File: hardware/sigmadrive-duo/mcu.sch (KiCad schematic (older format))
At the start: 107 parts, among them J1 CONN_02X02, J2 CONN_02X05, J3 Conn_02x03_Odd_Even, J4 CONN_02X02, J5 Conn_02x03_Odd_Even, J6 629_105_150_921, M1_SW1 CONN_02X02, M1_SW2 CONN_02X02, M2_SW1 CONN_02X02, M2_SW2 CONN_02X02, SW2 SW_DIP_x04, U12 SN65HVD75DGKR, U3 SN65HVD75DGKR, U4 TPD4S009, U5 STM32F745VGTx, U6 TPD4S009, U8 SN65HVD75DGKR, Y1 NX3225SA-12.000M-STD-CSR-1

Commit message: Sigmadrive-duo final HW update
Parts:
- R88: value 100 -> 120
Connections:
- net DRV_SDO: now also U5.17 (ADC1_IN12/ADC2_IN12/ADC3_IN12/ETH_TXD2/FMC_SDNE0/SPI2_MISO/USB_OTG_HS_ULPI_DIR/PC2); no longer U5.18 (ADC1_IN13/ADC2_IN13/ADC3_IN13/ETH_TX_CLK/FMC_SDCKE0/I2S2_SD/SPI2_MOSI/USB_OTG_HS_ULPI_NXT/PC3)
- net M1_IA_FB: now also U4.4 (D2+), U4.7 (D2+); no longer U4.1 (D1+), U4.10 (D1+)
- net M1_IC_FB: now also U4.1 (D1+), U4.10 (D1+); no longer U4.4 (D2+), U4.7 (D2+)
- net ADC1_IN4 renamed ADC3_IN3
- net ADC3_IN3: now also U5.25 (ADC1_IN3/ADC2_IN3/ADC3_IN3/ETH_COL/TIM2_CH4/TIM5_CH4/TIM9_CH2/USART2_RX/USB_OTG_HS_ULPI_D0/PA3); no longer U5.28 (ADC1_IN4/ADC2_IN4/DAC_OUT1/DCMI_HSYNC/I2S1_WS/I2S3_WS/SPI1_NSS/SPI3_NSS/USART2_CK/USB_OTG_HS_SOF/PA4)
- net PA3 renamed PA4
- net PA4: now also U5.28 (ADC1_IN4/ADC2_IN4/DAC_OUT1/DCMI_HSYNC/I2S1_WS/I2S3_WS/SPI1_NSS/SPI3_NSS/USART2_CK/USB_OTG_HS_SOF/PA4); no longer U5.25 (ADC1_IN3/ADC2_IN3/ADC3_IN3/ETH_COL/TIM2_CH4/TIM5_CH4/TIM9_CH2/USART2_RX/USB_OTG_HS_ULPI_D0/PA3)
- net PC2 renamed PC3
- net PC3: now also U5.18 (ADC1_IN13/ADC2_IN13/ADC3_IN13/ETH_TX_CLK/FMC_SDCKE0/I2S2_SD/SPI2_MOSI/USB_OTG_HS_ULPI_NXT/PC3); no longer U5.17 (ADC1_IN12/ADC2_IN12/ADC3_IN12/ETH_TXD2/FMC_SDNE0/SPI2_MISO/USB_OTG_HS_ULPI_DIR/PC2)
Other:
- note removed: "Swapped in Duo\nPE14 <--> PE15\n"
- moved on the sheet: R31, R43
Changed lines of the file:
@@
 Wire Wire Line
 	7200 13900 7200 14050
-Text HLabel 22300 3850 2    60   Input ~ 0
+Text HLabel 22300 3950 2    60   Input ~ 0
 M1_IC_FB
 Text HLabel 22300 3650 2    60   Input ~ 0
@@
 Text HLabel 22300 3750 2    60   Input ~ 0
 M1_IB_FB
-Text HLabel 18100 4150 2    60   Input ~ 0
+Text HLabel 18050 4150 2    60   Input ~ 0
 VBAT_ADC
 Text Label 17800 4450 2    60   ~ 0
@@
 P 12550 12550
 F 0 "R88" V 12630 12550 50  0000 C CNN
-F 1 "100" V 12550 12550 50  0000 C CNN
+F 1 "120" V 12550 12550 50  0000 C CNN
 F 2 "Resistor_SMD:R_0603_1608Metric" V 12480 12550 50  0001 C CNN
 F 3 "http://www.yageo.com.tw/exep/pages/download/literatures/PYu-R_INT-thick_7.pdf" H 12550 12550 50  0001 C CNN
@@
 Text HLabel 18050 6750 2    60   Output ~ 0
 DRV_SDI
-Text HLabel 18050 7250 2    60   Input ~ 0
+Text HLabel 18050 7150 2    60   Input ~ 0
 DRV_SDO
 Text HLabel 18050 8350 2    60   Output ~ 0
@@
 	3500 6650 5900 6650
 Wire Wire Line
-	16100 7250 18050 7250
+	16100 7150 18050 7150
 Wire Wire Line
 	16100 6750 18050 6750
@@
 L Device:R R31
 U 1 1 5CCA82C4
-P 19800 3850
-F 0 "R31" V 19850 3650 50  0000 C CNN
-F 1 "21" V 19800 3850 50  0000 C CNN
-F 2 "Resistor_SMD:R_0603_1608Metric" V 19730 3850 50  0001 C CNN
-F 3 "http://www.yageo.com.tw/exep/pages/download/literatures/PYu-R_INT-thick_7.pdf" H 19800 3850 50  0001 C CNN
-F 4 "311-21.0HRCT-ND" V 19800 3850 60  0001 C CNN "Part"
-F 5 "DigiKey" V 19800 3850 60  0001 C CNN "Provider"
-	1    19800 3850
+P 19800 3950
+F 0 "R31" V 19850 3750 50  0000 C CNN
+F 1 "21" V 19800 3950 50  0000 C CNN
+F 2 "Resistor_SMD:R_0603_1608Metric" V 19730 3950 50  0001 C CNN
+F 3 "http://www.yageo.com.tw/exep/pages/download/literatures/PYu-R_INT-thick_7.pdf" H 19800 3950 50  0001 C CNN
+F 4 "311-21.0HRCT-ND" V 19800 3950 60  0001 C CNN "Part"
+F 5 "DigiKey" V 19800 3950 60  0001 C CNN "Provider"
+	1    19800 3950
 	0    -1   -1   0
 $EndComp
@@
 $EndComp
 Wire Wire Line
-	16100 4150 18100 4150
-Wire Wire Line
-	16100 3850 19300 3850
-Wire Wire Line
-	19300 3150 19300 3850
-Connection ~ 19300 3850
-Wire Wire Line
-	19300 3850 19650 3850
+	16100 4150 18050 4150
 $Comp
 L power:+3V3 #PWR?
@@
 $EndComp
 Wire Wire Line
-	21750 2950 21750 3850
-Connection ~ 21750 3850
-Wire Wire Line
-	21750 3850 22300 3850
-Wire Wire Line
-	19950 3850 20400 3850
-Wire Wire Line
 	20300 3750 21850 3750
 Wire Wire Line
@@
 Wire Wire Line
 	20300 2850 20300 3750
-Wire Wire Line
-	20400 2950 20400 3850
-Connection ~ 20400 3850
-Wire Wire Line
-	20400 3850 21750 3850
 $Comp
 L Device:Crystal_GND24 Y1
@@
 Wire Wire Line
 	16100 7450 17800 7450
-Text HLabel 22300 7150 2    60   Input ~ 0
+Text HLabel 22300 7250 2    60   Input ~ 0
 M2_IC_FB
 Text HLabel 22300 6950 2    60   Input ~ 0
@@
 L Device:R R43
 U 1 1 600E0612
-P 19750 7150
-F 0 "R43" V 19800 6950 50  0000 C CNN
-F 1 "21" V 19750 7150 50  0000 C CNN
-F 2 "Resistor_SMD:R_0603_1608Metric" V 19680 7150 50  0001 C CNN
-F 3 "http://www.yageo.com.tw/exep/pages/download/literatures/PYu-R_INT-thick_7.pdf" H 19750 7150 50  0001 C CNN
-F 4 "311-21.0HRCT-ND" V 19750 7150 60  0001 C CNN "Part"
-F 5 "DigiKey" V 19750 7150 60  0001 C CNN "Provider"
-	1    19750 7150
+P 19750 7250
+F 0 "R43" V 19800 7050 50  0000 C CNN
+F 1 "21" V 19750 7250 50  0000 C CNN
+F 2 "Resistor_SMD:R_0603_1608Metric" V 19680 7250 50  0001 C CNN
+F 3 "http://www.yageo.com.tw/exep/pages/download/literatures/PYu-R_INT-thick_7.pdf" H 19750 7250 50  0001 C CNN
+F 4 "311-21.0HRCT-ND" V 19750 7250 60  0001 C CNN "Part"
+F 5 "DigiKey" V 19750 7250 60  0001 C CNN "Provider"
+	1    19750 7250
 	0    -1   -1   0
 $EndComp
@@
 	18500 6450 18500 6950
 Wire Wire Line
-	21750 6250 21750 7150
-Connection ~ 21750 7150
-Wire Wire Line
-	21750 7150 22300 7150
-Wire Wire Line
 	21950 6050 21950 6950
 Connection ~ 21950 6950
@@
 	21950 6950 22300 6950
 Wire Wire Line
-	19900 7150 20400 7150
-Wire Wire Line
 	20300 7050 21850 7050
 Wire Wire Line
@@
 	19900 6950 20200 6950
 Wire Wire Line
-	20400 6250 20400 7150
-Connection ~ 20400 7150
-Wire Wire Line
-	20400 7150 21750 7150
-Wire Wire Line
 	20200 6050 20200 6950
 Connection ~ 20200 6950
@@
 Wire Wire Line
 	16100 5950 17800 5950
-Wire Wire Line
-	16100 7150 19350 7150
-Wire Wire Line
-	19350 6450 19350 7150
-Connection ~ 19350 7150
-Wire Wire Line
-	19350 7150 19600 7150
 Text HLabel 3500 6450 0    60   Output ~ 0
 M1_CL
@@
 	16100 4350 16500 4350
 NoConn ~ 16100 4350
-Text Notes 1900 6800 0    60   ~ 0
-Swapped in Duo\nPE14 <--> PE15\n
 Text Label 17800 5850 2    60   ~ 0
 M1_QUAD_A
@@
 	16100 3650 18450 3650
 Wire Wire Line
-	19950 3650 20200 3650
-Wire Wire Line
 	18450 3150 18450 3650
 Connection ~ 18450 3650
 Wire Wire Line
 	18450 3650 19650 3650
+Text Label 17800 3850 2    60   ~ 0
+ADC3_IN3
 Wire Wire Line
-	20200 2750 20200 3650
-Connection ~ 20200 3650
-Wire Wire Line
-	20200 3650 21950 3650
-Wire Wire Line
-	21950 2750 21950 3650
-Connection ~ 21950 3650
-Wire Wire Line
-	21950 3650 22300 3650
-Text Label 17800 3950 2    60   ~ 0
-ADC1_IN4
-Wire Wire Line
-	16100 3950 17800 3950
+	16100 3850 17800 3850
 $Comp
 L Connector_Generic:Conn_02x05_Odd_Even GPIO1
@@
 	17100 11800 17600 11800
 Text Label 17600 11700 2    60   ~ 0
-ADC1_IN4
+ADC3_IN3
 Wire Wire Line
 	17100 11700 17600 11700
@@
 Wire Wire Line
 	17100 11900 17600 11900
+Wire Wire Line
+	16100 7250 19350 7250
+Wire Wire Line
+	19900 7250 20400 7250
+Wire Wire Line
+	21750 6250 21750 7250
+Connection ~ 21750 7250
+Wire Wire Line
+	21750 7250 22300 7250
+Wire Wire Line
+	20400 6250 20400 7250
+Connection ~ 20400 7250
+Wire Wire Line
+	20400 7250 21750 7250
+Wire Wire Line
+	19350 6450 19350 7250
+Connection ~ 19350 7250
+Wire Wire Line
+	19350 7250 19600 7250
+Wire Wire Line
+	19950 3650 20400 3650
+Wire Wire Line
+	20400 2950 20400 3650
+Connection ~ 20400 3650
+Wire Wire Line
+	20400 3650 21750 3650
+Wire Wire Line
+	21750 2950 21750 3650
+Connection ~ 21750 3650
+Wire Wire Line
+	21750 3650 22300 3650
+Wire Wire Line
+	16100 3950 19300 3950
+Wire Wire Line
+	19950 3950 20200 3950
+Wire Wire Line
+	20200 2750 20200 3950
+Connection ~ 20200 3950
+Wire Wire Line
+	21950 2750 21950 3950
+Wire Wire Line
+	20200 3950 21950 3950
+Connection ~ 21950 3950
+Wire Wire Line
+	21950 3950 22300 3950
+Wire Wire Line
+	19300 3150 19300 3950
+Connection ~ 19300 3950
+Wire Wire Line
+	19300 3950 19650 3950
 $EndSCHEMATC

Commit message: PCB sigmadrive-duo, version 3.6
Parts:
- removed C46: 4.7uF 50V, Capacitor_SMD:C_0805_2012Metric, symbol Device:C
- removed FB2: 0.6OHM/0.2A/2.2 kOhm, Resistor_SMD:R_0603_1608Metric, symbol Device:Ferrite_Bead
- added R37, R51: 10k, Resistor_SMD:R_0603_1608Metric, symbol Device:R
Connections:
- net +3.3VP is gone; now on net +3V3: C14.2, C19.2, C24.2, C28.1, C49.1, C54.2, C55.2, U5.100 (VDD), U5.11 (VDD), U5.27 (VDD), U5.50 (VDD), U5.6 (VBAT), U5.75 (VDD)
- net +3V3: now also J2.1 (Pin_1), R37.1, R51.1; no longer J2.3 (Pin_3)
- net DRV_FAULT: now also R51.2
- net DRV_SDO: now also R37.2
- net GND: now also J2.3 (Pin_3); no longer J2.1 (Pin_1)
- net M1_ENCODER_DE renamed ENCODER_DE_M2
- net M1_ENCODER_DI renamed ENCODER_DI_M2
- net M1_ENCODER_RO renamed ENCODER_RO_M2
- net M1_QUAD_A renamed PB6
- net M1_QUAD_B renamed PB7
- net M1_QUAD_Z renamed PD7
- net M1_TIM_CH3 renamed PB8
- net M2_ENCODER_DE renamed ENCODER_DE_M1
- net M2_ENCODER_DI renamed ENCODER_DI_M1
- net M2_ENCODER_RO renamed ENCODER_RO_M1
- net M2_QUAD_A renamed PB4
- net M2_QUAD_B renamed PB5
- net M2_QUAD_Z renamed PB11
- net M2_TIM_CH3 renamed PB0

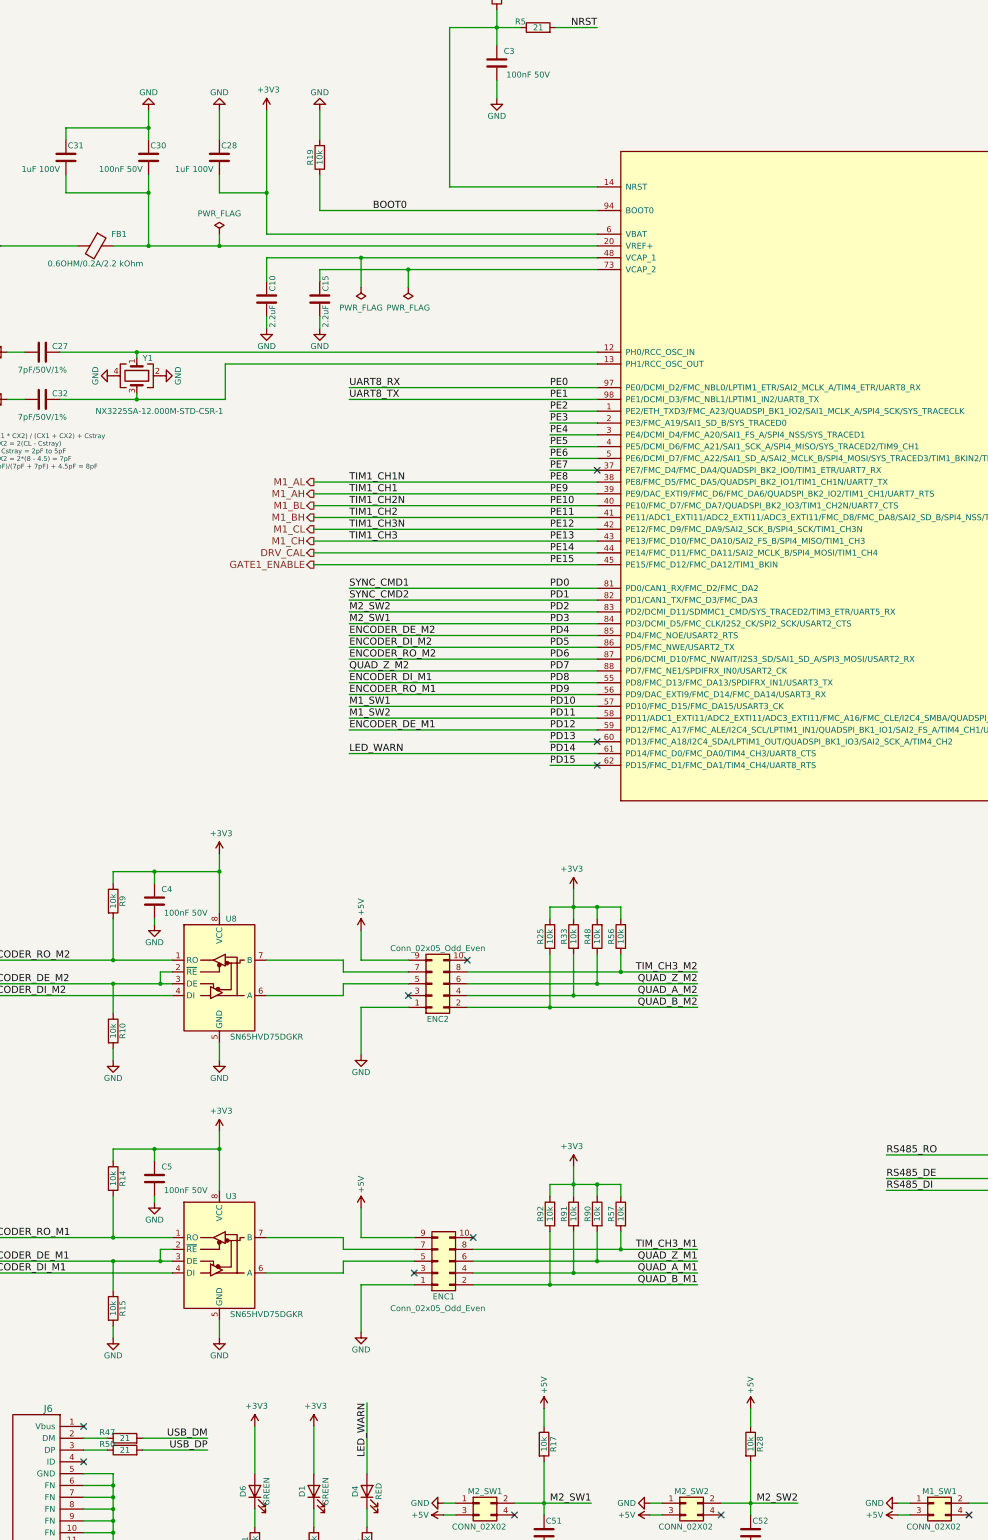
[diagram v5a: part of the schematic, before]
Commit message: Hardware version 3.8. Adde support for external battery.
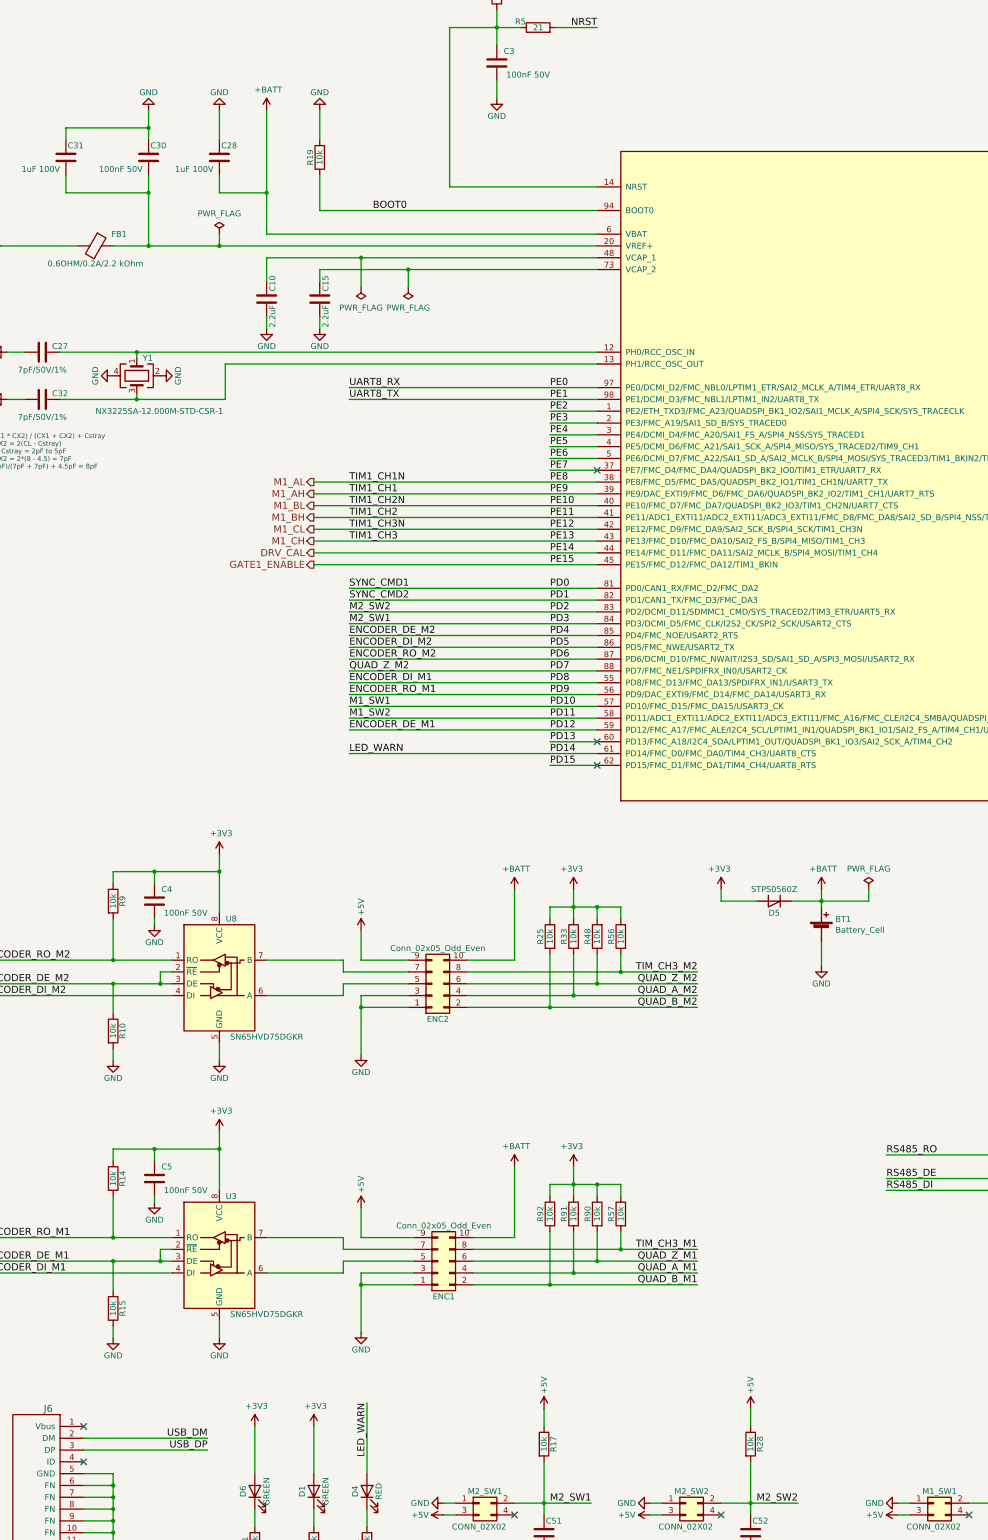
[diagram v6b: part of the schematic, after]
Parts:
- removed R47, R50: 21, Resistor_SMD:R_0603_1608Metric, symbol Device:R
- added BT1: Battery_Cell, Battery:Battery_Panasonic_CR1220-VCN_Vertical_CircularHoles, symbol Device:Battery_Cell
- added D5: STPS0560Z, Diode_SMD:D_SOD-123, symbol Device:D_Shockley
- ENC1, ENC2: Part (none) -> H10247-ND; Provider (none) -> DigiKey
- J3, J5: Part (none) -> H2866-ND; Provier (none) -> DigiKey
- M1_SW1, M1_SW2, M2_SW1, M2_SW2: Part 732-5374-ND -> H10244-ND
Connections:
- net +3V3: now also D5.2 (A); no longer C28.1, U5.6 (VBAT)
- net GND: now also ENC1.3 (Pin_3), ENC2.3 (Pin_3), BT1.2 (-)
- net PA11: now also J6.2 (DM)
- net PA12: now also J6.3 (DP)
- net +BATT: now reaches ENC2.10 (Pin_10)
- net +BATT: now also C28.1, ENC1.10 (Pin_10), U5.6 (VBAT), BT1.1 (+), D5.1 (K)
- no-connect marks 22 -> 18

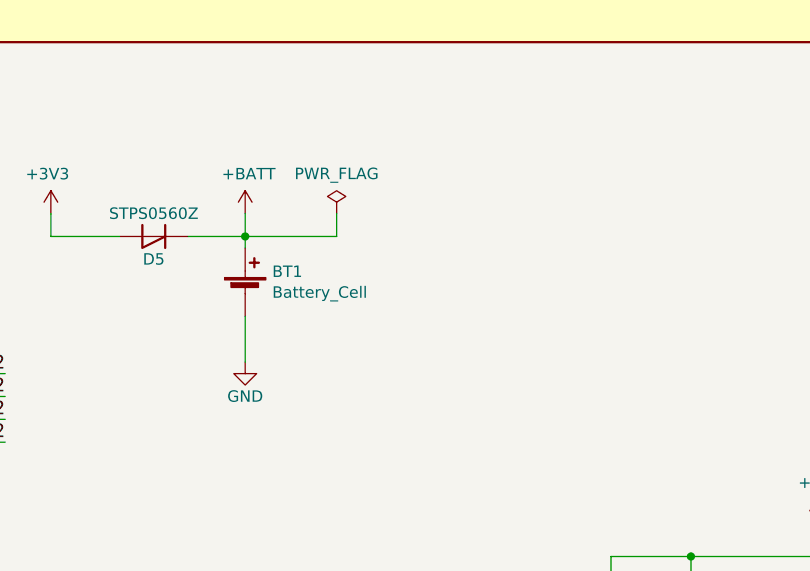
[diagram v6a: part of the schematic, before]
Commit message: Hardware version 3.8. Adde support for external battery.
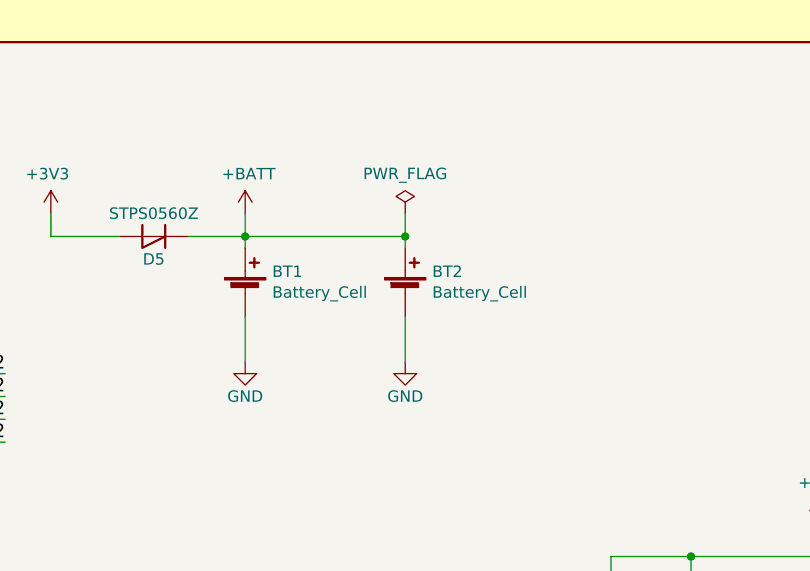
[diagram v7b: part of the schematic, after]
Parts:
- added BT2: Battery_Cell, Battery:Battery_Panasonic_CR1220-VCN_Vertical_CircularHoles, symbol Device:Battery_Cell
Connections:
- net +BATT: now also BT2.1 (+)
- net GND: now also BT2.2 (-)
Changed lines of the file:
@@
 L power:PWR_FLAG #FLG01
 U 1 1 5FBCF26B
-P 8200 9500
-F 0 "#FLG01" H 8200 9575 50  0001 C CNN
-F 1 "PWR_FLAG" H 8200 9674 50  0000 C CNN
-F 2 "" H 8200 9500 50  0001 C CNN
-F 3 "" H 8200 9500 50  0001 C CNN
-	1    8200 9500
+P 8500 9500
+F 0 "#FLG01" H 8500 9575 50  0001 C CNN
+F 1 "PWR_FLAG" H 8500 9674 50  0000 C CNN
+F 2 "" H 8500 9500 50  0001 C CNN
+F 3 "" H 8500 9500 50  0001 C CNN
+	1    8500 9500
 	1    0    0    -1
 $EndComp
 Wire Wire Line
-	7800 9600 8200 9600
+	7800 9600 8500 9600
 Wire Wire Line
-	8200 9600 8200 9500
+	8500 9600 8500 9500
 $Comp
 L power:+BATT #PWR0117
@@
 Wire Wire Line
 	1550 14250 2600 14250
+$Comp
+L Device:Battery_Cell BT2
+U 1 1 5F6E911C
+P 8500 9850
+F 0 "BT2" H 8618 9946 50  0000 L CNN
+F 1 "Battery_Cell" H 8618 9855 50  0000 L CNN
+F 2 "Battery:Battery_Panasonic_CR1220-VCN_Vertical_CircularHoles" V 8500 9910 50  0001 C CNN
+F 3 "~" V 8500 9910 50  0001 C CNN
+F 4 "VL-1220/VCN" H 8500 9850 50  0001 C CNN "Part"
+F 5 "PANASONIC" H 8500 9850 50  0001 C CNN "Provider"
+	1    8500 9850
+	1    0    0    -1
+$EndComp
+Wire Wire Line
+	8500 9650 8500 9600
+Connection ~ 8500 9600
+$Comp
+L power:GND #PWR0165
+U 1 1 5F736ED2
+P 8500 10150
+F 0 "#PWR0165" H 8500 9900 50  0001 C CNN
+F 1 "GND" H 8500 10000 50  0000 C CNN
+F 2 "" H 8500 10150 50  0001 C CNN
+F 3 "" H 8500 10150 50  0001 C CNN
+	1    8500 10150
+	1    0    0    -1
+$EndComp
+Wire Wire Line
+	8500 9950 8500 10150
 $EndSCHEMATC
